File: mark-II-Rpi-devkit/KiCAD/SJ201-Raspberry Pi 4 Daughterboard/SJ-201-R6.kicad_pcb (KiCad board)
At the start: 4 copper layers, 67 x 98 mm, 235 parts, among them J1 Barrel_Jack, J10 Conn_01x04, J13 USB-PinHeader, J2 AudioJack2_Ground, J3 SPK, J4 SPK, J5 PowerTP, J6 Raspberry_Pi_4, J7 FanConnector, J8 PWR, J9 RotaryEncoder, Q1 MMBT3904, Q2 BSS138, Q3 AO3401A, Q4 BSS138, Q5 BSS138, Q6 BSS138, SW1 MuteMic, U1 XL4501E1, U10 SPK0641HT4H-1, U11 SPK0641HT4H-1, U12 TPS75933KTTR, U13 ATtiny1614-SS, U15 AMS1117-1.8, U16 UDA1334ATS, U2 CoralTPU, U3 TAS5806MD, U4 AMS1117-3.3, U5 SN74LVC125APWR, U7 MP2359, U8 XMOS-XVF3510, U9 DNP - AT25SFxx 16mb or greater, X1 SG-210STF 24M

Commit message: Updated files for R6 v2
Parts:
- C2, C9: value 100NF -> 100NF-DNP
- C65: value 10UF -> 10UF-DNP
- C66: value 1uF -> 1uF-DNP
- C67: value 470uF -> 470uF-DNP
- C68: value 10UF -> 10uF-DNP
- C69: value 22UF -> 22UF-DNP
- Q2, Q4, Q5, Q6: value BSS138 -> BSS138-DNP
- R10: value 0R -> 0R-DNP
- R23, R30: value 33R -> 33R-DNP
- R29, R37, R54, R55, R56, R58, R59, R60: value 10k -> 10k-DNP
- R51: value 3.3K -> 3.3K-DNP
- U12: value TPS75933KTTR -> TPS75933KTTR-DNP
- U15: value AMS1117-1.8 -> AMS1117-1.8-DNP
- U2: value CoralTPU -> CoralTPU-DNP
- U8: footprint user:QFN-60-1EP_7x7mm_P0.4mm_EP5.6x5.6mm-HandSolder -> user:QFN-60-1EP_7x7mm_P0.4mm_EP5.6x5.6mm
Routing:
- net +3V3: track 134.5 -> 133.4 mm
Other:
- board text added: "Mycroft MK2 SJ-201-R6.02"
- board text removed: "Mycroft MK2 SJ-201-R6"

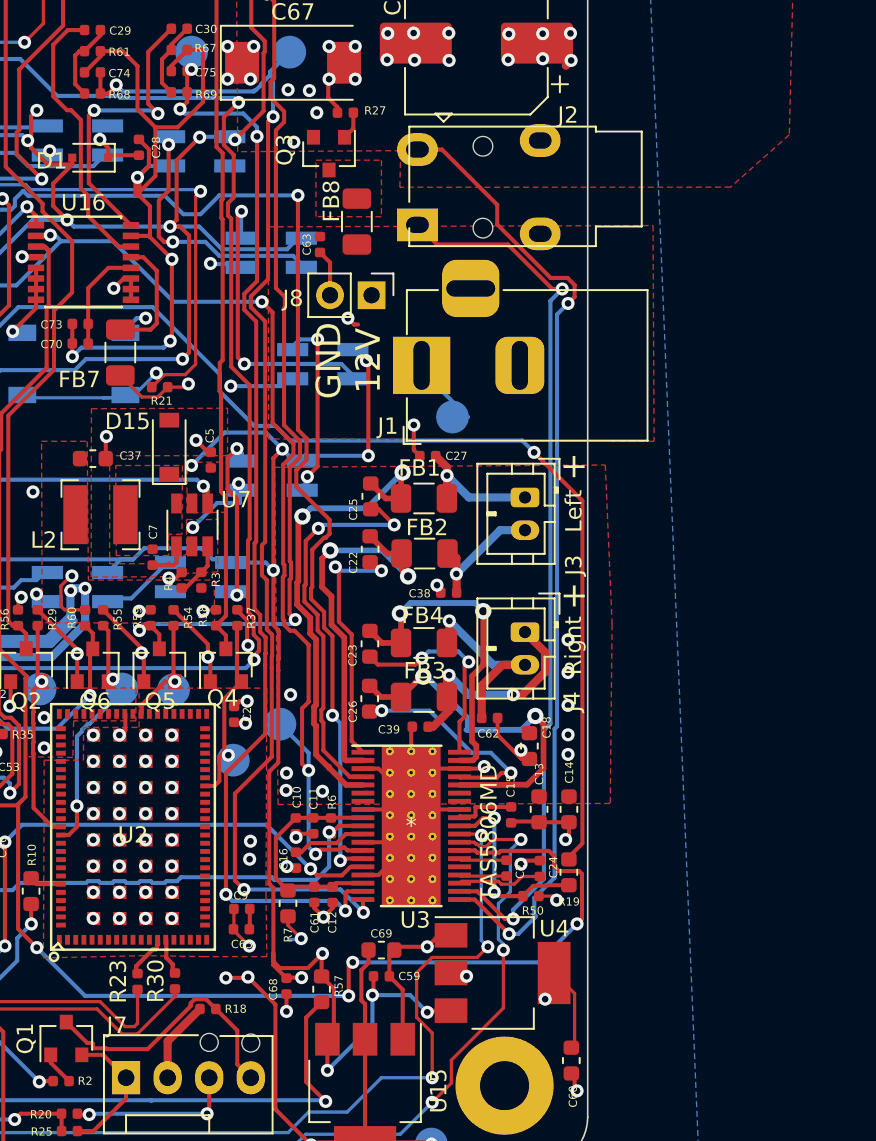
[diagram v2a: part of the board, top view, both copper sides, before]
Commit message: Update libraries, reorganize files
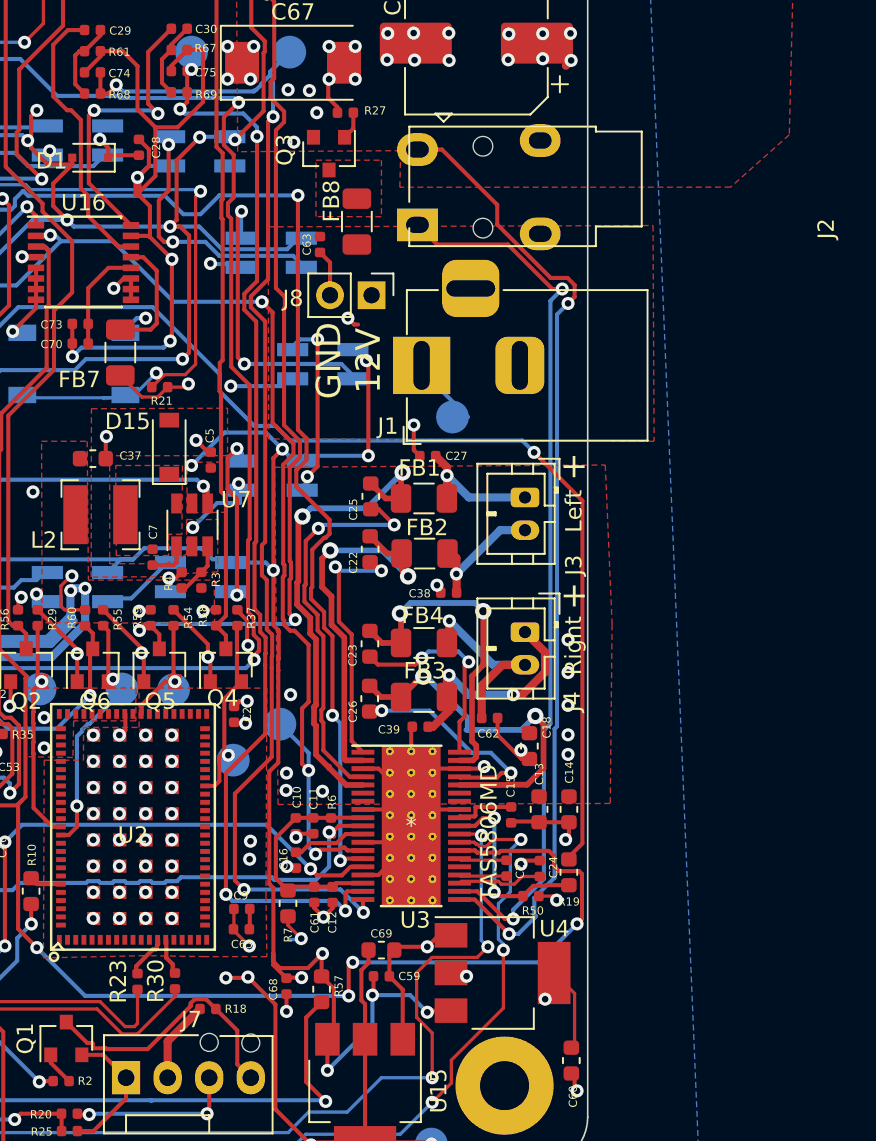
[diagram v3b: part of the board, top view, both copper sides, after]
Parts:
- D10, D11, D12, D13, D2, D3, D4, D5, D6, D7, D8, D9: footprint user:LED_WS2812_Mini_3.5x3.5mm_P1.1mm -> Mycroft:LED_WS2812_Mini_3.5x3.5mm_P1.1mm
- H5: footprint mycroft:mycroft_logo_graphic -> Logos:mycroft_logo_graphic
- H6: footprint libraries:simon-jestor-logo -> Logos:simon-jester-logo
- H7: footprint mycroft:mycroft_logo_words -> Logos:mycroft_logo_words
- J2: footprint user:Jack_3.5mm_PJ-3210 -> Mycroft:Jack_3.5mm_PJ-3210
- J7: footprint user:FanPinHeader_1x04_P2.54mm_Vertical -> Mycroft:FanPinHeader_1x04_P2.54mm_Vertical
- U10, U11: footprint user:HCLGA-MP34DT05 -> Mycroft:HCLGA-MP34DT05
- U2: footprint user:CoralTPU -> CoralTPU:CoralTPU
- U8: footprint user:QFN-60-1EP_7x7mm_P0.4mm_EP5.6x5.6mm -> XMOS:QFN-60-1EP_7x7mm_P0.4mm_EP5.6x5.6mm
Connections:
- D13 pad 2: (no net) -> Net-(D13-Pad2)
- D20 pad 2: (no net) -> Net-(D20-Pad2)
- J6 pad 1: (no net) -> Net-(J6-Pad1)
- J6 pad 17: (no net) -> Net-(J6-Pad17)
- U2 pad 78: (no net) -> Net-(U2-Pad78)
- U2 pad 82: (no net) -> Net-(U2-Pad82)
- U3 pad 24: (no net) -> Net-(U3-Pad24)
- U5 pad 11: (no net) -> Net-(U5-Pad11)
- U8 pad 23: (no net) -> Net-(U8-Pad23)
- U8 pad 24: (no net) -> Net-(U8-Pad24)
- U8 pad 25: (no net) -> Net-(U8-Pad25)
- U8 pad 30: (no net) -> Net-(U8-Pad30)
- U8 pad 32: (no net) -> Net-(U8-Pad32)
- U8 pad 37: (no net) -> Net-(U8-Pad37)
- U8 pad 44: (no net) -> Net-(U8-Pad44)
- U8 pad 47: (no net) -> Net-(U8-Pad47)
- U8 pad 49: (no net) -> Net-(U8-Pad49)
